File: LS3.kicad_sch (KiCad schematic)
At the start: 6 parts, among them Q5 NCE4080K, Q6 NCE4080K, Q7 NCE4080K

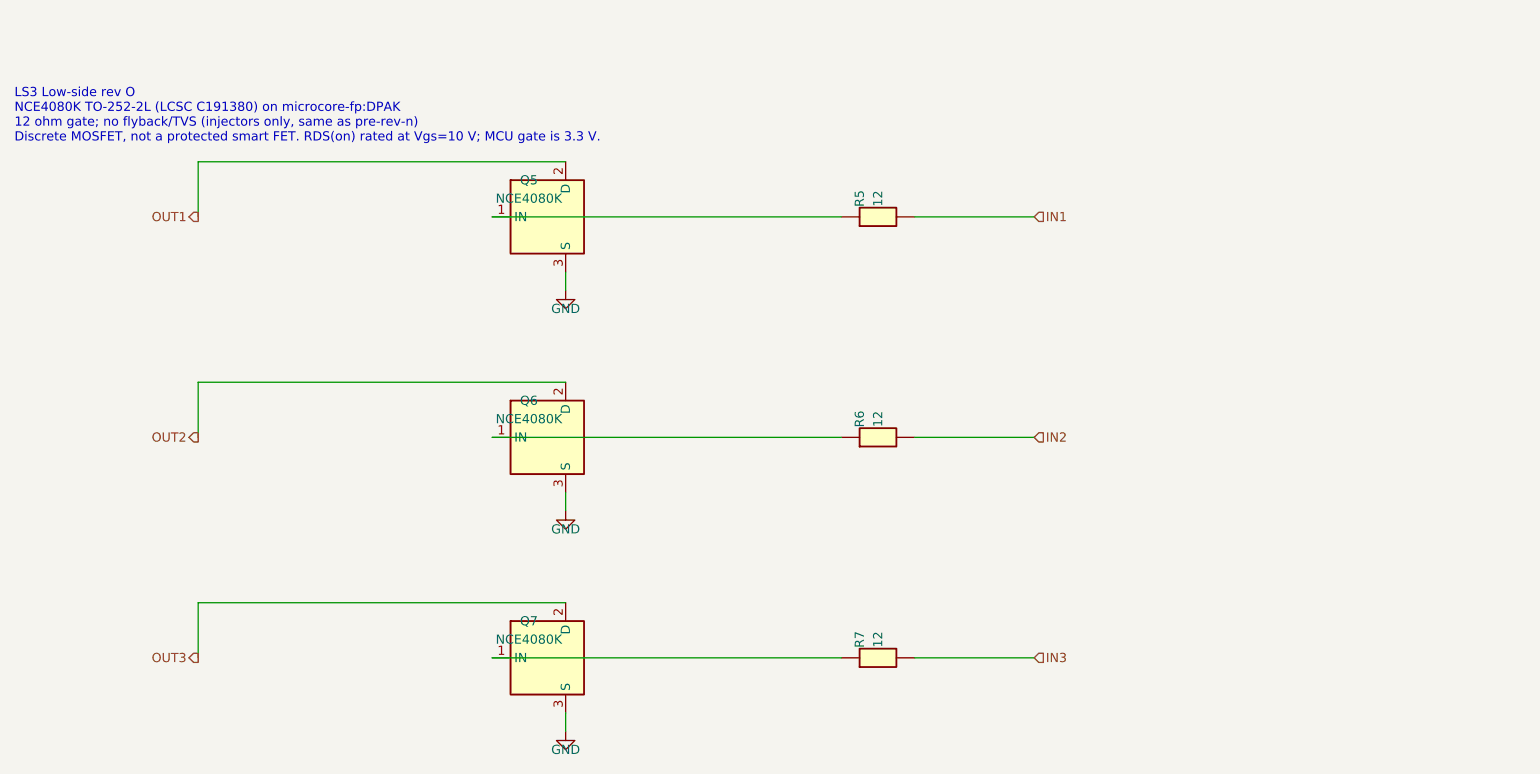
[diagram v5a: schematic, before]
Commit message: Rev p: AOD4184A on Q1-Q7, LS flyback+TVS, frame short fixes
Quintin chose AOD4184A (LCSC C99124) plus TVS for budget and reliability.
Q5-Q7 get the existing US1M flyback and SMAJ33A. Injector/VR frame shorts
on the board copper are cleared; Hellen module pad-G noise stays documented.

Co-authored-by: Quintin <quintinbannink42@users.noreply.github.com>
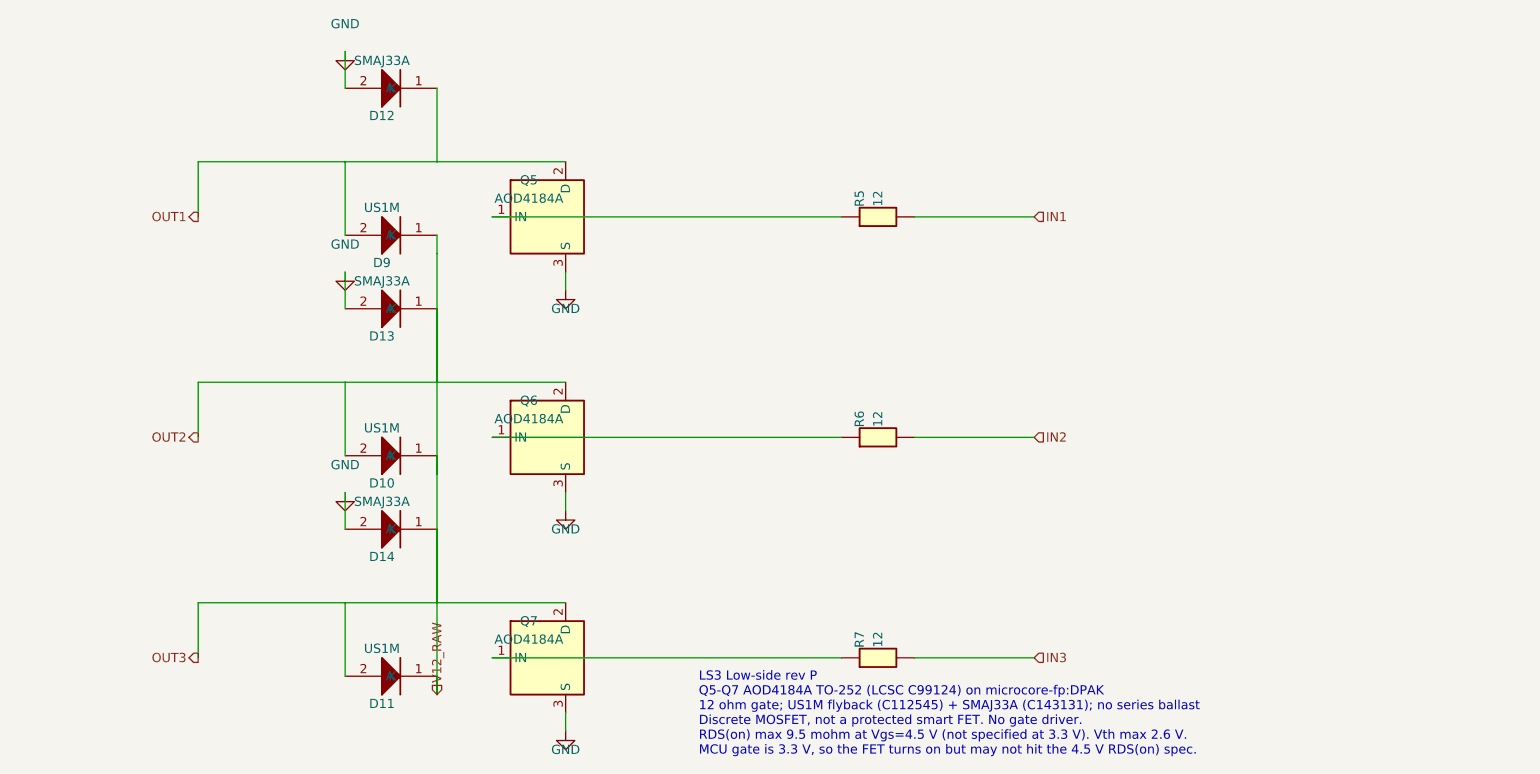
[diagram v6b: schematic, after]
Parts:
- added D10, D11, D9: US1M, microcore-fp:DO214AC, symbol hellen-one-common:1N4148WS
- added D12, D13, D14: SMAJ33A, microcore-fp:DO214AC, symbol hellen-one-common:1N4148WS
- Q5, Q6, Q7: value NCE4080K -> AOD4184A
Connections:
- net OUT3 is gone; now on net OUT2: Q7.2 (D)
- net GND: now also D12.2 (A), D13.2 (A), D14.2 (A)
- net OUT1: now also D12.1 (K), D9.2 (A)
- net OUT2: now also D10.1 (K), D10.2 (A), D11.1 (K), D11.2 (A), D13.1 (K), D14.1 (K), D9.1 (K)
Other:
- note added: "LS3 Low-side rev P Q5-Q7 AOD4184A TO-252 (LCSC C99124) on microcore-fp:DPAK 12 ohm gate; US1M flyback (C112545) + SMAJ33A (C143131); no series ballast Discrete MOSFET, not a protected smart FET. No gate driver. RDS(on) max 9.5 mohm at Vgs=4.5 V (not specified at 3.3 V). Vth max 2.6 V. MCU gate is 3.3 V, so the FET turns on but may not hit the 4.5 V RDS(on) spec."
- note removed: "LS3 Low-side rev O NCE4080K TO-252-2L (LCSC C191380) on microcore-fp:DPAK 12 ohm gate; no flyback/TVS (injectors only, same as pre-rev-n) Discrete MOSFET, not a protected smart FET. RDS(on) rated at Vgs=10 V; MCU gate is 3.3 V."

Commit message: Rev p: keep Q1-Q7 as NCE4080K; LS US1M+SMAJ33A stays
Budget and reliability first. No FET or BOM upgrade and no DPAK land change. Low-side clamps stay the injector US1M and SMAJ33A already in the BOM.

Co-authored-by: Quintin <quintinbannink42@users.noreply.github.com>
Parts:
- Q5, Q6, Q7: value AOD4184A -> NCE4080K
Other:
- note added: "LS3 Low-side rev P Q5-Q7 stay NCE4080K TO-252 (LCSC C191380) on microcore-fp:DPAK 12 ohm gate; US1M flyback (C112545) + SMAJ33A (C143131); no series ballast Discrete MOSFET, not a protected smart FET. No gate driver. No premium clamps. RDS(on) < 7 mohm at Vgs=10 V, ID=20 A. No RDS(on) row at 4.5 V or 2.5 V. Vth 1.2/1.8/2.5 V. MCU gate is 3.3 V, so the FET turns on but is not at the 10 V RDS(on) s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"
- note removed: "LS3 Low-side rev P Q5-Q7 AOD4184A TO-252 (LCSC C99124) on microcore-fp:DPAK 12 ohm gate; US1M flyback (C112545) + SMAJ33A (C143131); no series ballast Discrete MOSFET, not a protected smart FET. No gate driver. RDS(on) max 9.5 mohm at Vgs=4.5 V (not specified at 3.3 V). Vth max 2.6 V. MCU gate is 3.3 V, so the FET turns on but may not hit the 4.5 V RDS(on) spec."
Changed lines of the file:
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@@
 		(rev "P")
 		(company "Core EFI")
-		(comment 1 "rev p: Q5-Q7 AOD4184A C99124; US1M flyback + SMAJ33A")
-		(comment 2 "RDS(on) at 4.5 V; Vth max 2.6 V; MCU gate 3.3 V; no gate driver")
+		(comment 1 "rev p: Q5-Q7 stay NCE4080K C191380; US1M flyback + SMAJ33A")
+		(comment 2 "RDS(on) at 10 V only; Vth max 2.5 V; MCU gate 3.3 V; no gate driver")
 	)
 	(symbol
@@
 			)
 		)
-		(property "Value" "AOD4184A"
+		(property "Value" "NCE4080K"
 			(at 96.52 22.86 0)
 			(effects
@@
 			)
 		)
-		(property "Value" "AOD4184A"
+		(property "Value" "NCE4080K"
 			(at 96.52 53.339999999999996 0)
 			(effects
@@
 			)
 		)
-		(property "Value" "AOD4184A"
+		(property "Value" "NCE4080K"
 			(at 96.52 83.82 0)
 			(effects
@@
 		)
 	)
-	(text "LS3 Low-side rev P\nQ5-Q7 AOD4184A TO-252 (LCSC C99124) on microcore-fp:DPAK\n12 ohm gate; US1M flyback (C112545) + SMAJ33A (C143131); no series ballast\nDiscrete MOSFET, not a protected smart FET. No gate driver.\nRDS(on) max 9.5 mohm at Vgs=4.5 V (not specified at 3.3 V). Vth max 2.6 V.\nMCU gate is 3.3 V, so the FET turns on but may not hit the 4.5 V RDS(on) spec."
+	(text "LS3 Low-side rev P\nQ5-Q7 stay NCE4080K TO-252 (LCSC C191380) on microcore-fp:DPAK\n12 ohm gate; US1M flyback (C112545) + SMAJ33A (C143131); no series ballast\nDiscrete MOSFET, not a protected smart FET. No gate driver. No premium clamps.\nRDS(on) < 7 mohm at Vgs=10 V, ID=20 A. No RDS(on) row at 4.5 V or 2.5 V.\nVth 1.2/1.8/2.5 V. MCU gate is 3.3 V, so the FET turns on but is not at the 10 V RDS(on) spec."
 		(at 120 100 0)
 		(effects
